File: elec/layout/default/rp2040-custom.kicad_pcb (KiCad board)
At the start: 2 copper layers, 40 x 40 mm, 28 parts

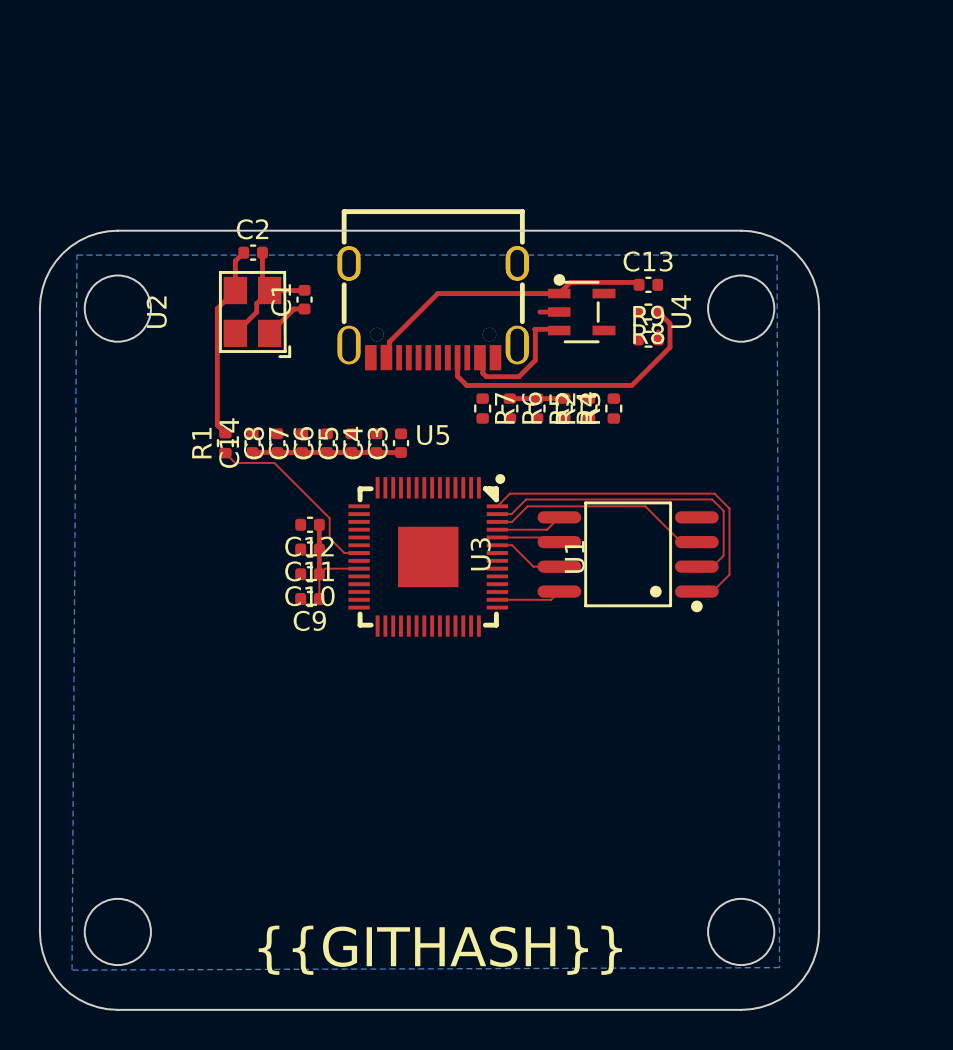
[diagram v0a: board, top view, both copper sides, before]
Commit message: Add initial layout and wiring
This will most likely change as the design evolves
But I wanted to try the auto layout capabilities
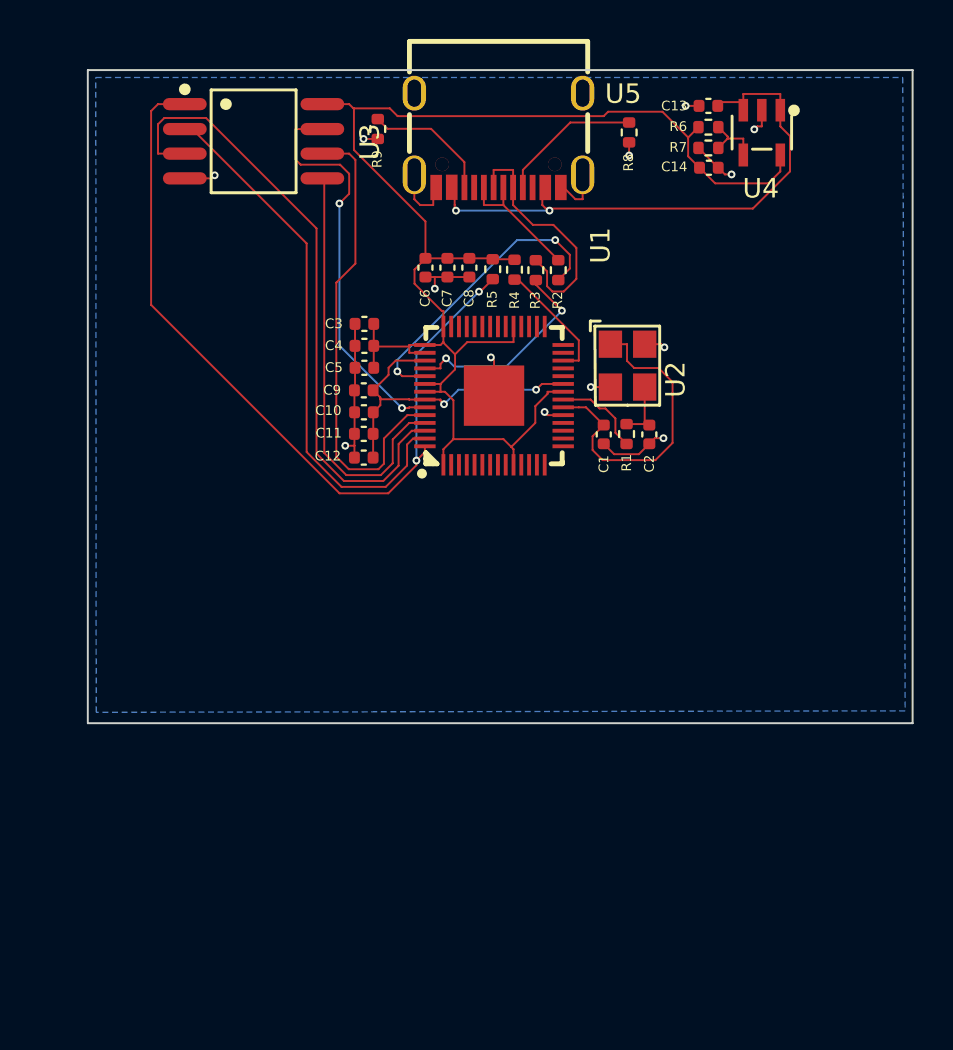
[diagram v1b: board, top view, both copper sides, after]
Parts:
- moved U3 28.6 mm to (123.4, 79.2), turned to -90 degrees
- moved C14 27.4 mm to (146.7, 80.6), turned to 0 degrees
- moved C2 22.4 mm to (143.7, 94.3), turned to -90 degrees
- moved R1 20.6 mm to (142.5, 94.3)
- moved U2 19.4 mm to (142.6, 90.8), turned to -90 degrees
- moved R7 17.7 mm to (146.7, 79.6), turned to 180 degrees
- moved R6 17.7 mm to (146.7, 78.5), turned to 0 degrees
- moved R9 17.6 mm to (129.7, 78.6), turned to -90 degrees
- moved C1 16.8 mm to (141.3, 94.3), turned to -90 degrees
- moved C8 13.4 mm to (134.4, 85.7), turned to -90 degrees
- moved U4 13.1 mm to (149.5, 78.8), turned to 180 degrees
- moved C7 11.7 mm to (133.3, 85.7), turned to -90 degrees
- moved C9 11.1 mm to (129.0, 92.0)
- moved C6 10.3 mm to (132.2, 85.7), turned to -90 degrees
- moved C13 9.69 mm to (146.7, 77.4), turned to 180 degrees
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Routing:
- net vcc: track 13.8 -> 75.7 mm
- net cs: track 17.9 -> 42.2 mm, vias 0 -> 2
- net gnd: track 10.1 -> 32.5 mm, vias 0 -> 13
- net io2: track 11.3 -> 32.9 mm
- net sck: track 3.28 -> 24.2 mm
- net io0: track 3.44 -> 21.6 mm
- net io3: track 3.64 -> 20.8 mm, vias 0 -> 2
- net usb_dp: track 0.00 -> 15.4 mm, vias 0 -> 2
- net xin: track 2.31 -> 16.3 mm
- net dm: track 0.00 -> 12.9 mm
- net io1: track 16.1 -> 27.9 mm
- net vcc-1: track 5.97 -> 17.2 mm, vias 0 -> 2
- net usb_dm: track 0.00 -> 10.9 mm, vias 0 -> 2
- net vcc-2: track 21.8 -> 29.5 mm, vias 0 -> 2
- net cc1: track 14.9 -> 7.37 mm
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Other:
- board size 40 x 40 mm -> 42.3 x 33.5 mm
- board text removed: "{{GITHASH}}"

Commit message: Initial refactor RP2040kit
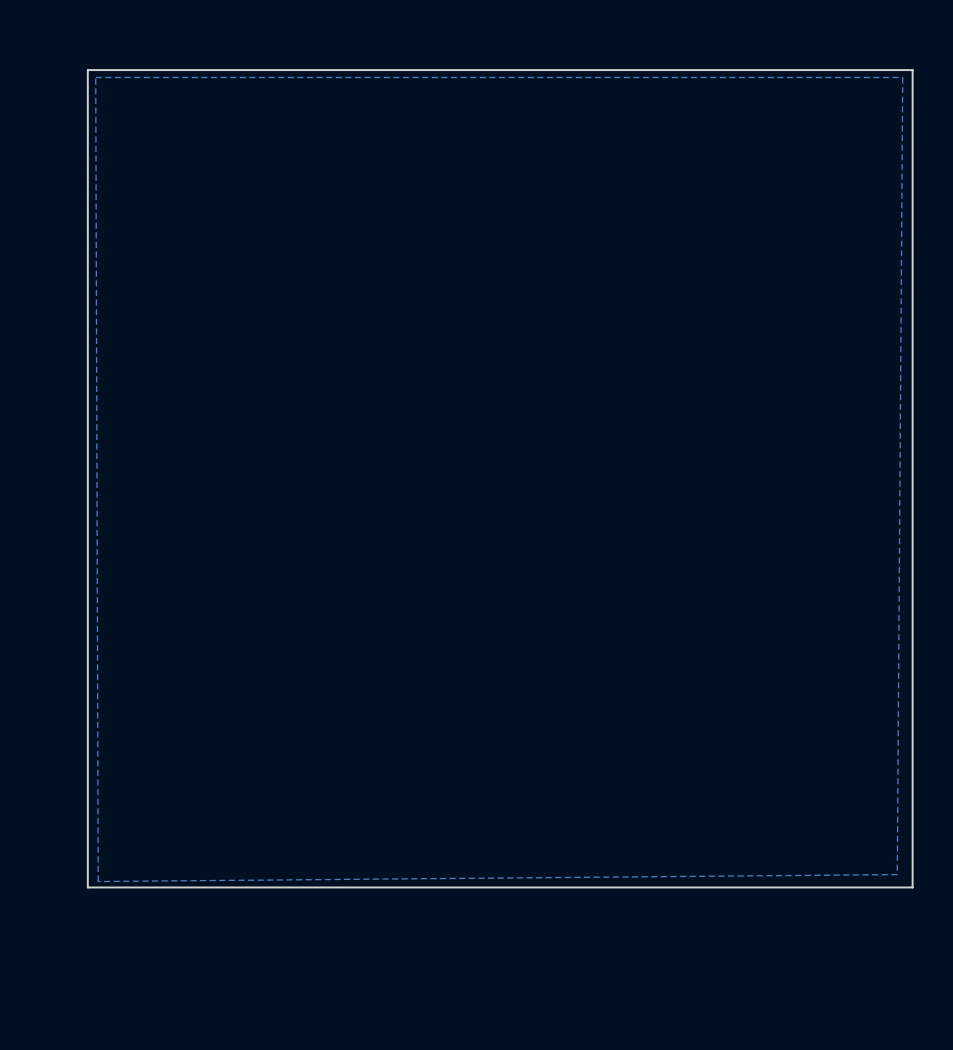
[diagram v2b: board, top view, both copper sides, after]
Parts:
- removed C1, C2: Multilayer Ceramic Capacitors MLCC - SMD/SMT 20pF 50V 0402 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, lib:C0402
- removed C10, C11, C3, C4, C5, C6, C7, C9: Multilayer Ceramic Capacitors MLCC - SMD/SMT 100nF 10V 0402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, lib:C0402
- removed C12, C13, C14, C8: Multilayer Ceramic Capacitors MLCC - SMD/SMT 1uF 6.3V 0402 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, lib:C0402
- removed R1: Chip Resistor - Surface Mount 1KOhms ±5% 1/16W 0402 RoHS, lib:R0402
- removed R2, R3: Chip Resistor - Surface Mount 27KOhms ±5% 1/16W 0402 RoHS, lib:R0402
- removed R4, R5, R7: Chip Resistor - Surface Mount 10KOhms ±5% 1/16W 0402 RoHS, lib:R0402
- removed R6: Chip Resistor - Surface Mount 18KOhms ±5% 1/16W 0402 RoHS, lib:R0402
- removed R8, R9: Chip Resistor - Surface Mount 4.7KOhms ±5% 1/16W 0402 RoHS, lib:R0402
- removed U1: , lib:LQFN-56_L7.0-W7.0-P0.4-EP
- removed U2: , lib:OSC-SMD_4P-L3.2-W2.5-BL
- removed U3: , lib:SOIC-8_L5.3-W5.3-P1.27-LS8.0-BL
- removed U4: , lib:SOT-23-5_L3.0-W1.7-P0.95-LS2.8-BL
- removed U5: , lib:USB-C-SMD_KH-TYPE-C-16P
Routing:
- net vcc: track 75.7 -> 0.00 mm
- net cs: track 42.2 -> 0.00 mm, vias 2 -> 0
- net io2: track 32.9 -> 0.00 mm
- net gnd: track 32.5 -> 0.00 mm, vias 13 -> 0
- net vcc-2: track 29.5 -> 0.00 mm, vias 2 -> 0
- net io1: track 27.9 -> 0.00 mm
- net sck: track 24.2 -> 0.00 mm
- net io0: track 21.6 -> 0.00 mm
- net io3: track 20.8 -> 0.00 mm, vias 2 -> 0
- net vcc-1: track 17.2 -> 0.00 mm, vias 2 -> 0
- net xin: track 16.3 -> 0.00 mm
- net usb_dp: track 15.4 -> 0.00 mm, vias 2 -> 0
- net dm: track 12.9 -> 0.00 mm
- net usb_dm: track 10.9 -> 0.00 mm, vias 2 -> 0
- net cc1: track 7.37 -> 0.00 mm
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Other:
- board size 42.3 x 33.5 mm -> 42.3 x 42 mm
